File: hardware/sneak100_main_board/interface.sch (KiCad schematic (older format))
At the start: 18 parts, among them J10 Conn_01x06, SW2 SW_Push, SW3 SW_Push, SW4 SW_Push, U10 SSD1306, U11 TSOP4838

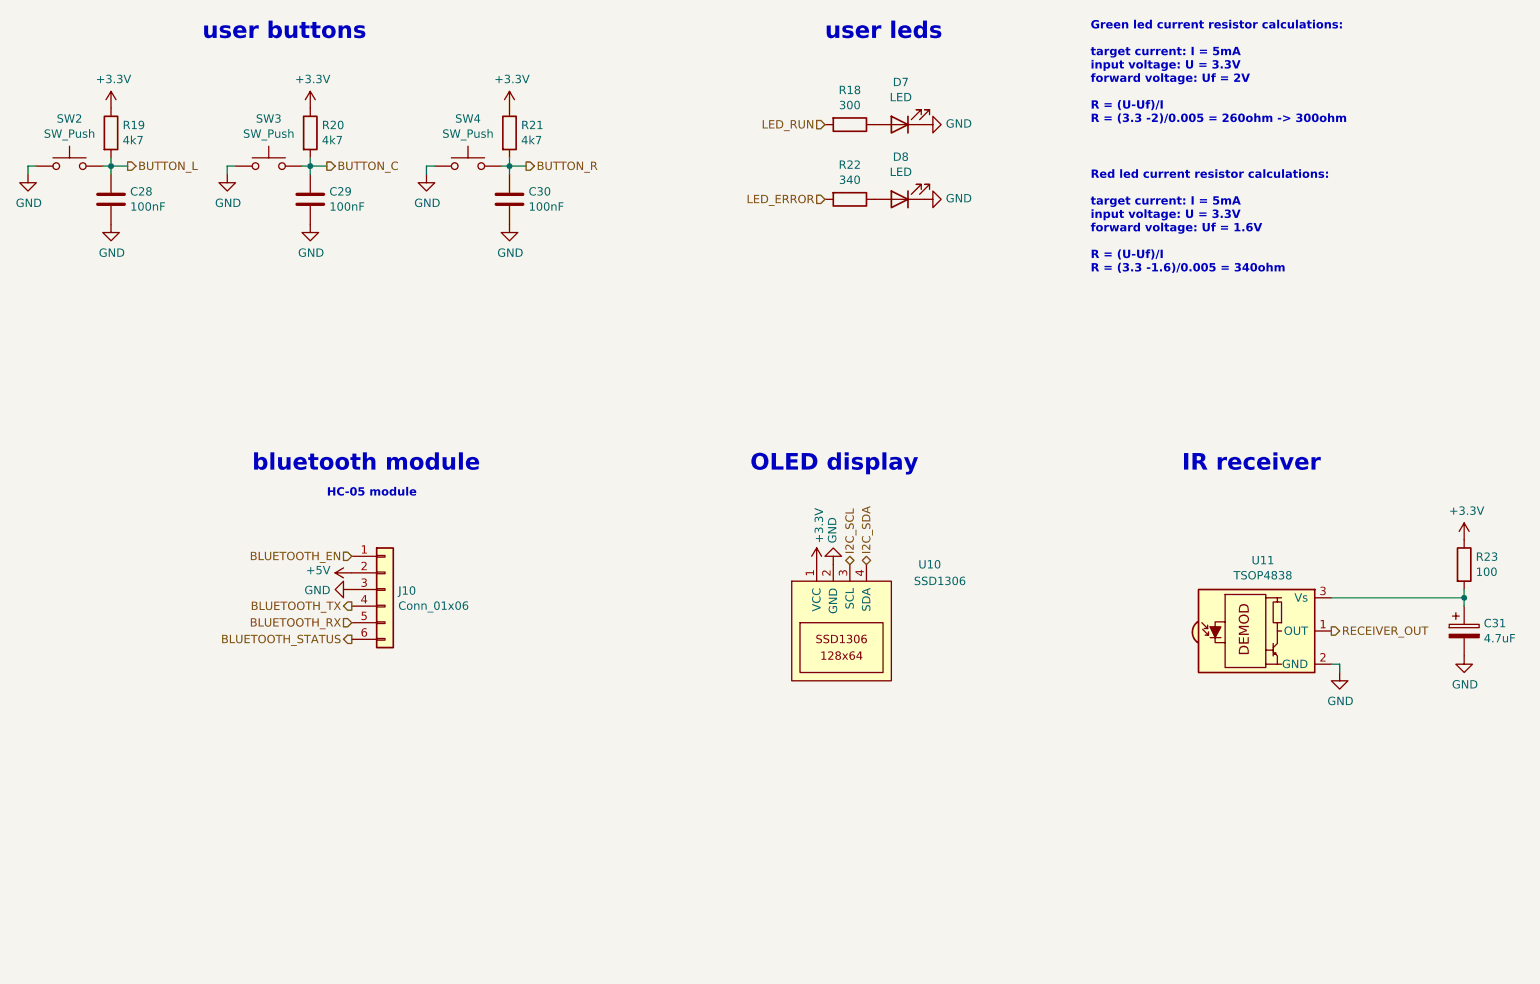
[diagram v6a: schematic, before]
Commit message: Add external proximity sensor, erase old from schematic
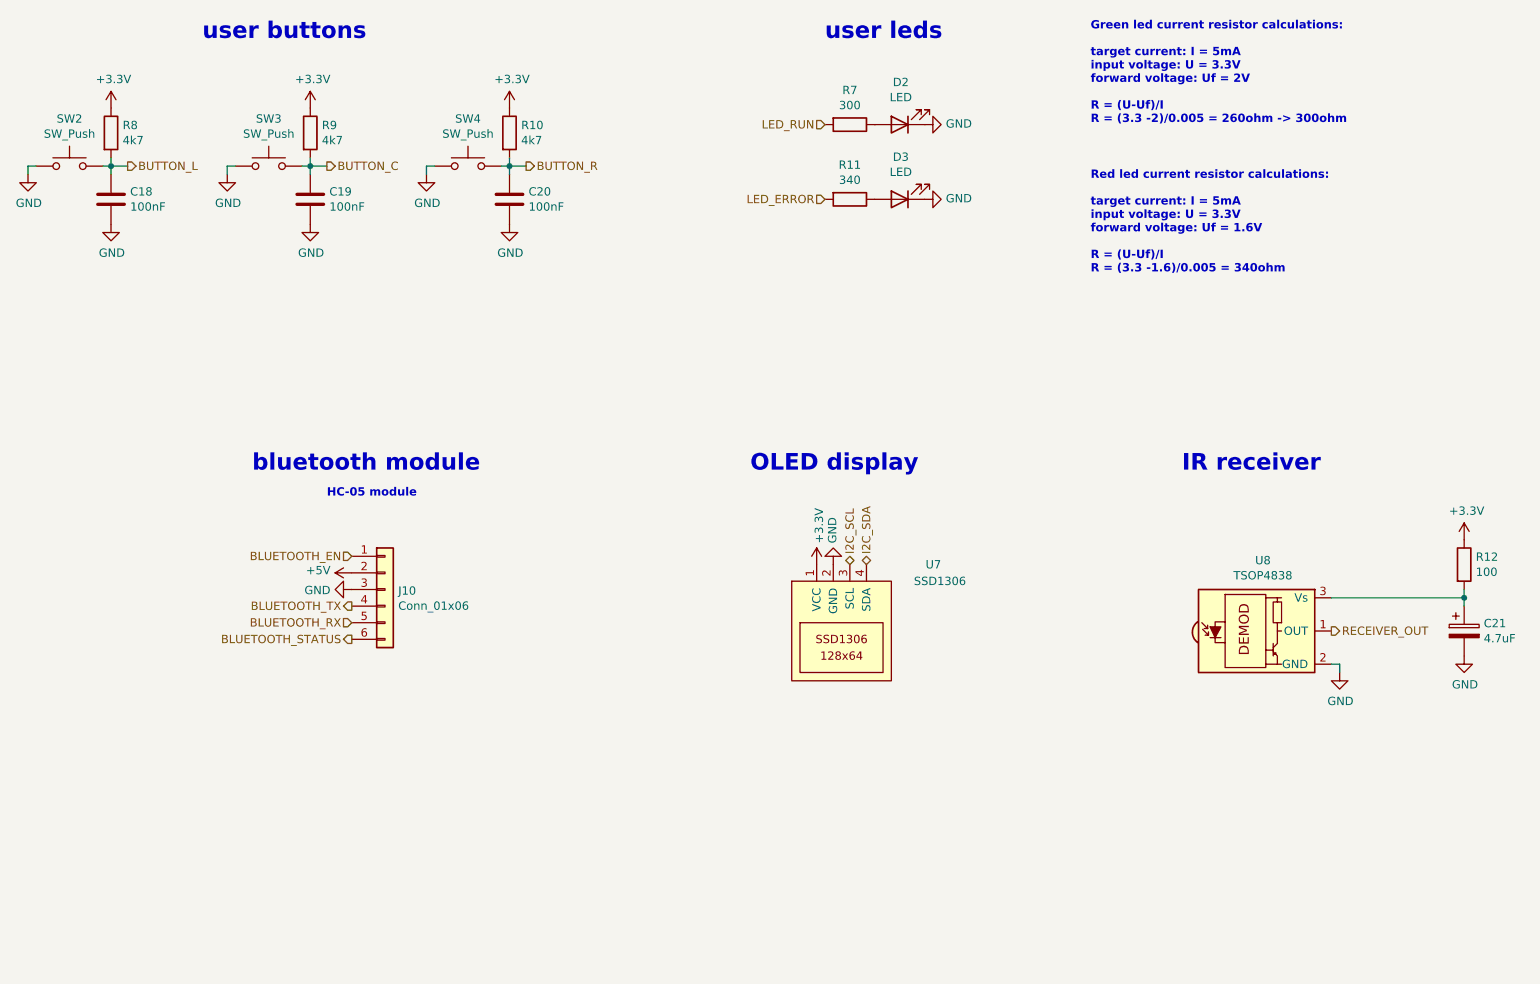
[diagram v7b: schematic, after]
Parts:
- C21: renamed from C31; footprint Capacitor_THT:CP_Radial_D5.0mm_P2.00mm -> Capacitor_Tantalum_SMD:CP_EIA-3216-18_Kemet-A
- renumbered C28 to C18, C29 to C19, C30 to C20, D7 to D2, D8 to D3, R21 to R10, R22 to R11, R23 to R12, R18 to R7, R19 to R8, R20 to R9, U10 to U7, U11 to U8
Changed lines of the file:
@@
 $Descr A4 11693 8268
 encoding utf-8
-Sheet 7 7
+Sheet 5 7
 Title ""
 Date ""
@@
 $EndComp
 $Comp
-L Device:R R19
+L Device:R R8
 U 1 1 61055001
 P 1700 1700
-F 0 "R19" H 1770 1746 50  0000 L CNN
+F 0 "R8" H 1770 1746 50  0000 L CNN
 F 1 "4k7" H 1770 1655 50  0000 L CNN
 F 2 "Resistor_SMD:R_0603_1608Metric" V 1630 1700 50  0001 C CNN
@@
 $EndComp
 $Comp
-L power:+3.3V #PWR0110
+L power:+3.3V #PWR061
 U 1 1 610558C1
 P 1700 1550
-F 0 "#PWR0110" H 1700 1400 50  0001 C CNN
+F 0 "#PWR061" H 1700 1400 50  0001 C CNN
 F 1 "+3.3V" H 1715 1723 50  0000 C CNN
 F 2 "" H 1700 1550 50  0001 C CNN
@@
 $EndComp
 $Comp
-L power:GND #PWR0114
+L power:GND #PWR065
 U 1 1 61055FD5
 P 1200 1950
-F 0 "#PWR0114" H 1200 1700 50  0001 C CNN
+F 0 "#PWR065" H 1200 1700 50  0001 C CNN
 F 1 "GND" H 1205 1777 50  0000 C CNN
 F 2 "" H 1200 1950 50  0001 C CNN
@@
 $EndComp
 $Comp
-L Device:C C28
+L Device:C C18
 U 1 1 61056486
 P 1700 2100
-F 0 "C28" H 1815 2146 50  0000 L CNN
+F 0 "C18" H 1815 2146 50  0000 L CNN
 F 1 "100nF" H 1815 2055 50  0000 L CNN
 F 2 "Capacitor_SMD:C_0603_1608Metric" H 1738 1950 50  0001 C CNN
@@
 $EndComp
 $Comp
-L power:GND #PWR0118
+L power:GND #PWR069
 U 1 1 6105698D
 P 1700 2250
-F 0 "#PWR0118" H 1700 2000 50  0001 C CNN
+F 0 "#PWR069" H 1700 2000 50  0001 C CNN
 F 1 "GND" H 1705 2077 50  0000 C CNN
 F 2 "" H 1700 2250 50  0001 C CNN
@@
 BUTTON_L
 $Comp
-L Device:LED D7
+L Device:LED D2
 U 1 1 6105F07D
 P 6450 1650
-F 0 "D7" H 6443 1395 50  0000 C CNN
+F 0 "D2" H 6443 1395 50  0000 C CNN
 F 1 "LED" H 6443 1486 50  0000 C CNN
 F 2 "LED_SMD:LED_0603_1608Metric" H 6450 1650 50  0001 C CNN
@@
 $EndComp
 $Comp
-L Device:R R18
+L Device:R R7
 U 1 1 61060DB0
 P 6150 1650
-F 0 "R18" V 5943 1650 50  0000 C CNN
+F 0 "R7" V 5943 1650 50  0000 C CNN
 F 1 "300" V 6034 1650 50  0000 C CNN
 F 2 "Resistor_SMD:R_0603_1608Metric" V 6080 1650 50  0001 C CNN
@@
 $EndComp
 $Comp
-L power:GND #PWR0113
+L power:GND #PWR064
 U 1 1 61061E6F
 P 6600 1650
-F 0 "#PWR0113" H 6600 1400 50  0001 C CNN
+F 0 "#PWR064" H 6600 1400 50  0001 C CNN
 F 1 "GND" V 6605 1522 50  0000 R CNN
 F 2 "" H 6600 1650 50  0001 C CNN
@@
 BLUETOOTH_TX
 $Comp
-L power:GND #PWR0126
+L power:GND #PWR076
 U 1 1 60F1FEEB
 P 3150 4450
-F 0 "#PWR0126" H 3150 4200 50  0001 C CNN
+F 0 "#PWR076" H 3150 4200 50  0001 C CNN
 F 1 "GND" V 3155 4322 50  0000 R CNN
 F 2 "" H 3150 4450 50  0001 C CNN
@@
 $EndComp
 $Comp
-L power:+5V #PWR0125
+L power:+5V #PWR075
 U 1 1 60F200B0
 P 3150 4350
-F 0 "#PWR0125" H 3150 4200 50  0001 C CNN
+F 0 "#PWR075" H 3150 4200 50  0001 C CNN
 F 1 "+5V" V 3165 4478 50  0000 L CNN
 F 2 "" H 3150 4350 50  0001 C CNN
@@
 IR receiver
 $Comp
-L Sneak100_kicad:TSOP4838 U11
+L Sneak100_kicad:TSOP4838 U8
 U 1 1 60F76D5D
 P 8600 4700
-F 0 "U11" H 8638 5125 50  0000 C CNN
+F 0 "U8" H 8638 5125 50  0000 C CNN
 F 1 "TSOP4838" H 8638 5034 50  0000 C CNN
 F 2 "Connector_PinHeader_2.54mm:PinHeader_1x03_P2.54mm_Vertical" H 8600 5050 50  0001 C CNN
@@
 $EndComp
 $Comp
-L power:GND #PWR0128
+L power:GND #PWR078
 U 1 1 60F7CCD5
 P 9100 4950
-F 0 "#PWR0128" H 9100 4700 50  0001 C CNN
+F 0 "#PWR078" H 9100 4700 50  0001 C CNN
 F 1 "GND" H 9105 4777 50  0000 C CNN
 F 2 "" H 9100 4950 50  0001 C CNN
@@
 $EndComp
 $Comp
-L Device:CP C31
+L Device:CP C21
 U 1 1 60F7F945
 P 9850 4700
-F 0 "C31" H 9968 4746 50  0000 L CNN
+F 0 "C21" H 9968 4746 50  0000 L CNN
 F 1 "4.7uF" H 9968 4655 50  0000 L CNN
-F 2 "Capacitor_THT:CP_Radial_D5.0mm_P2.00mm" H 9888 4550 50  0001 C CNN
+F 2 "Capacitor_Tantalum_SMD:CP_EIA-3216-18_Kemet-A" H 9888 4550 50  0001 C CNN
 F 3 "~" H 9850 4700 50  0001 C CNN
 	1    9850 4700
@@
 $EndComp
 $Comp
-L power:GND #PWR0127
+L power:GND #PWR077
 U 1 1 60F80FC7
 P 9850 4850
-F 0 "#PWR0127" H 9850 4600 50  0001 C CNN
+F 0 "#PWR077" H 9850 4600 50  0001 C CNN
 F 1 "GND" H 9855 4677 50  0000 C CNN
 F 2 "" H 9850 4850 50  0001 C CNN
@@
 $EndComp
 $Comp
-L Device:R R23
+L Device:R R12
 U 1 1 60F8B46D
 P 9850 4300
-F 0 "R23" H 9920 4346 50  0000 L CNN
+F 0 "R12" H 9920 4346 50  0000 L CNN
 F 1 "100" H 9920 4255 50  0000 L CNN
 F 2 "Resistor_SMD:R_0603_1608Metric" V 9780 4300 50  0001 C CNN
@@
 $EndComp
 $Comp
-L power:+3.3V #PWR0122
+L power:+3.3V #PWR072
 U 1 1 60F8BCE9
 P 9850 4150
-F 0 "#PWR0122" H 9850 4000 50  0001 C CNN
+F 0 "#PWR072" H 9850 4000 50  0001 C CNN
 F 1 "+3.3V" H 9865 4323 50  0000 C CNN
 F 2 "" H 9850 4150 50  0001 C CNN
@@
 $EndComp
 $Comp
-L Device:R R20
+L Device:R R9
 U 1 1 60F90EC5
 P 2900 1700
-F 0 "R20" H 2970 1746 50  0000 L CNN
+F 0 "R9" H 2970 1746 50  0000 L CNN
 F 1 "4k7" H 2970 1655 50  0000 L CNN
 F 2 "Resistor_SMD:R_0603_1608Metric" V 2830 1700 50  0001 C CNN
@@
 $EndComp
 $Comp
-L power:+3.3V #PWR0111
+L power:+3.3V #PWR062
 U 1 1 60F90ECB
 P 2900 1550
-F 0 "#PWR0111" H 2900 1400 50  0001 C CNN
+F 0 "#PWR062" H 2900 1400 50  0001 C CNN
 F 1 "+3.3V" H 2915 1723 50  0000 C CNN
 F 2 "" H 2900 1550 50  0001 C CNN
@@
 $EndComp
 $Comp
-L power:GND #PWR0115
+L power:GND #PWR066
 U 1 1 60F90ED1
 P 2400 1950
-F 0 "#PWR0115" H 2400 1700 50  0001 C CNN
+F 0 "#PWR066" H 2400 1700 50  0001 C CNN
 F 1 "GND" H 2405 1777 50  0000 C CNN
 F 2 "" H 2400 1950 50  0001 C CNN
@@
 $EndComp
 $Comp
-L Device:C C29
+L Device:C C19
 U 1 1 60F90ED7
 P 2900 2100
-F 0 "C29" H 3015 2146 50  0000 L CNN
+F 0 "C19" H 3015 2146 50  0000 L CNN
 F 1 "100nF" H 3015 2055 50  0000 L CNN
 F 2 "Capacitor_SMD:C_0603_1608Metric" H 2938 1950 50  0001 C CNN
@@
 $EndComp
 $Comp
-L power:GND #PWR0119
+L power:GND #PWR070
 U 1 1 60F90EDD
 P 2900 2250
-F 0 "#PWR0119" H 2900 2000 50  0001 C CNN
+F 0 "#PWR070" H 2900 2000 50  0001 C CNN
 F 1 "GND" H 2905 2077 50  0000 C CNN
 F 2 "" H 2900 2250 50  0001 C CNN
@@
 $EndComp
 $Comp
-L Device:R R21
+L Device:R R10
 U 1 1 60F92AB2
 P 4100 1700
-F 0 "R21" H 4170 1746 50  0000 L CNN
+F 0 "R10" H 4170 1746 50  0000 L CNN
 F 1 "4k7" H 4170 1655 50  0000 L CNN
 F 2 "Resistor_SMD:R_0603_1608Metric" V 4030 1700 50  0001 C CNN
@@
 $EndComp
 $Comp
-L power:+3.3V #PWR0112
+L power:+3.3V #PWR063
 U 1 1 60F92AB8
 P 4100 1550
-F 0 "#PWR0112" H 4100 1400 50  0001 C CNN
+F 0 "#PWR063" H 4100 1400 50  0001 C CNN
 F 1 "+3.3V" H 4115 1723 50  0000 C CNN
 F 2 "" H 4100 1550 50  0001 C CNN
@@
 $EndComp
 $Comp
-L power:GND #PWR0116
+L power:GND #PWR067
 U 1 1 60F92ABE
 P 3600 1950
-F 0 "#PWR0116" H 3600 1700 50  0001 C CNN
+F 0 "#PWR067" H 3600 1700 50  0001 C CNN
 F 1 "GND" H 3605 1777 50  0000 C CNN
 F 2 "" H 3600 1950 50  0001 C CNN
@@
 $EndComp
 $Comp
-L Device:C C30
+L Device:C C20
 U 1 1 60F92AC4
 P 4100 2100
-F 0 "C30" H 4215 2146 50  0000 L CNN
+F 0 "C20" H 4215 2146 50  0000 L CNN
 F 1 "100nF" H 4215 2055 50  0000 L CNN
 F 2 "Capacitor_SMD:C_0603_1608Metric" H 4138 1950 50  0001 C CNN
@@
 $EndComp
 $Comp
-L power:GND #PWR0120
+L power:GND #PWR071
 U 1 1 60F92ACA
 P 4100 2250
-F 0 "#PWR0120" H 4100 2000 50  0001 C CNN
+F 0 "#PWR071" H 4100 2000 50  0001 C CNN
 F 1 "GND" H 4105 2077 50  0000 C CNN
 F 2 "" H 4100 2250 50  0001 C CNN
@@
 BUTTON_R
 $Comp
-L power:+3.3V #PWR0123
+L power:+3.3V #PWR073
 U 1 1 60FBF32E
 P 5950 4300
-F 0 "#PWR0123" H 5950 4150 50  0001 C CNN
+F 0 "#PWR073" H 5950 4150 50  0001 C CNN
 F 1 "+3.3V" V 5965 4428 50  0000 L CNN
 F 2 "" H 5950 4300 50  0001 C CNN
@@
 $EndComp
 $Comp
-L power:GND #PWR0124
+L power:GND #PWR074
 U 1 1 60FBFC20
 P 6050 4300
-F 0 "#PWR0124" H 6050 4050 50  0001 C CNN
+F 0 "#PWR074" H 6050 4050 50  0001 C CNN
 F 1 "GND" V 6055 4172 50  0000 R CNN
 F 2 "" H 6050 4300 50  0001 C CNN
@@
 $EndComp
 $Comp
-L Device:LED D8
+L Device:LED D3
 U 1 1 60FD241C
 P 6450 2100
-F 0 "D8" H 6443 1845 50  0000 C CNN
+F 0 "D3" H 6443 1845 50  0000 C CNN
 F 1 "LED" H 6443 1936 50  0000 C CNN
 F 2 "LED_SMD:LED_0603_1608Metric" H 6450 2100 50  0001 C CNN
@@
 $EndComp
 $Comp
-L Device:R R22
+L Device:R R11
 U 1 1 60FD2422
 P 6150 2100
-F 0 "R22" V 5943 2100 50  0000 C CNN
+F 0 "R11" V 5943 2100 50  0000 C CNN
 F 1 "340" V 6034 2100 50  0000 C CNN
 F 2 "Resistor_SMD:R_0603_1608Metric" V 6080 2100 50  0001 C CNN
@@
 $EndComp
 $Comp
-L power:GND #PWR0117
+L power:GND #PWR068
 U 1 1 60FD2428
 P 6600 2100
-F 0 "#PWR0117" H 6600 1850 50  0001 C CNN
+F 0 "#PWR068" H 6600 1850 50  0001 C CNN
 F 1 "GND" V 6605 1972 50  0000 R CNN
 F 2 "" H 6600 2100 50  0001 C CNN
@@
 HC-05 module
 $Comp
-L Sneak100_kicad:SSD1306 U10
+L Sneak100_kicad:SSD1306 U7
 U 1 1 6101ACF5
 P 6100 4650
-F 0 "U10" H 6700 5000 50  0000 R CNN
+F 0 "U7" H 6700 5000 50  0000 R CNN
 F 1 "SSD1306" H 6850 4900 50  0000 R CNN
 F 2 "sneak100_lib:SSD1306_module" H 5950 4600 50  0001 C CNN

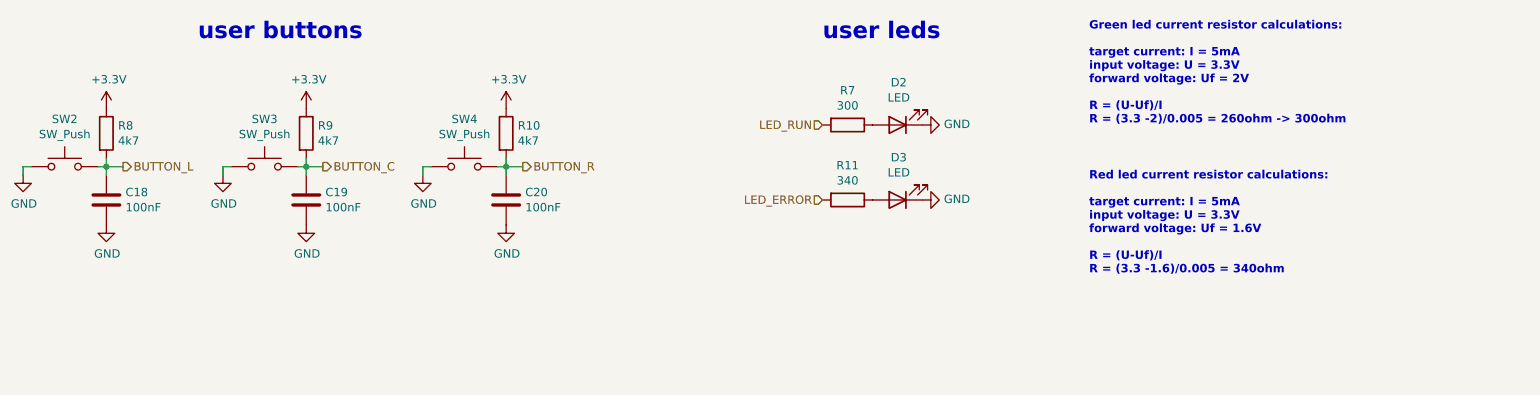
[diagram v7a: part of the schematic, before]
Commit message: component list and values fix
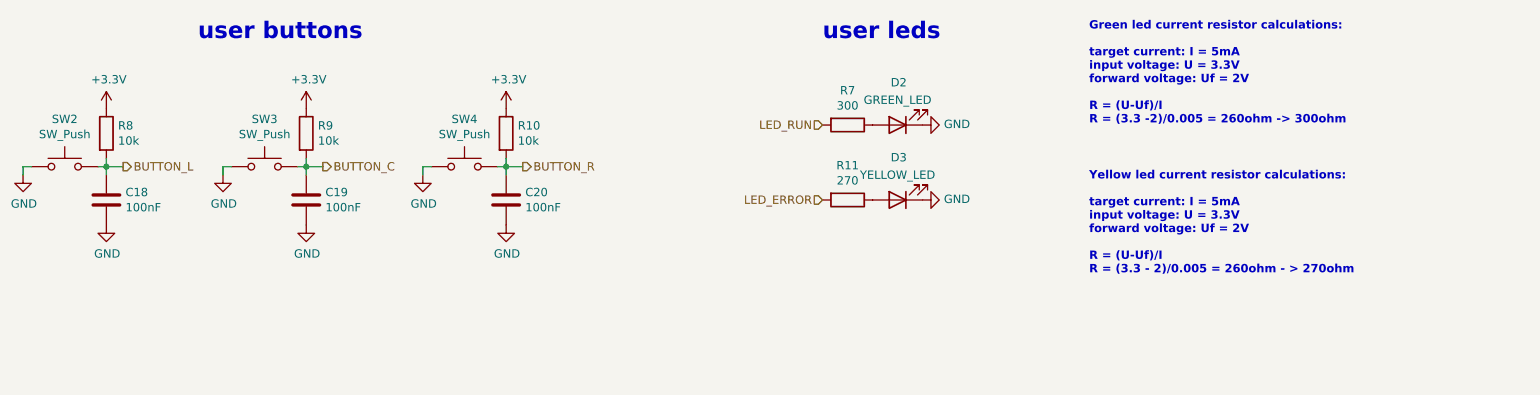
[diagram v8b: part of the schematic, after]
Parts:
- D2: value LED -> GREEN_LED
- D3: value LED -> YELLOW_LED
- R10, R8, R9: value 4k7 -> 10k
- R11: value 340 -> 270
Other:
- note added: "Yellow led current resistor calculations:\n\ntarget current: I = 5mA\ninput voltage: U = 3.3V\nforward voltage: Uf = 2V\n\nR = (U-Uf)/I\nR = (3.3 - 2)/0.005 = 260ohm - > 270ohm"
- note removed: "Red led current resistor calculations:\n\ntarget current: I = 5mA\ninput voltage: U = 3.3V\nforward voltage: Uf = 1.6V\n\nR = (U-Uf)/I\nR = (3.3 -1.6)/0.005 = 340ohm"
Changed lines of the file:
@@
 P 1700 1700
 F 0 "R8" H 1770 1746 50  0000 L CNN
-F 1 "4k7" H 1770 1655 50  0000 L CNN
+F 1 "10k" H 1770 1655 50  0000 L CNN
 F 2 "Resistor_SMD:R_0603_1608Metric" V 1630 1700 50  0001 C CNN
 F 3 "~" H 1700 1700 50  0001 C CNN
@@
 P 6450 1650
 F 0 "D2" H 6443 1395 50  0000 C CNN
-F 1 "LED" H 6443 1486 50  0000 C CNN
+F 1 "GREEN_LED" H 6450 1500 50  0000 C CNN
 F 2 "LED_SMD:LED_0603_1608Metric" H 6450 1650 50  0001 C CNN
 F 3 "~" H 6450 1650 50  0001 C CNN
@@
 P 2900 1700
 F 0 "R9" H 2970 1746 50  0000 L CNN
-F 1 "4k7" H 2970 1655 50  0000 L CNN
+F 1 "10k" H 2970 1655 50  0000 L CNN
 F 2 "Resistor_SMD:R_0603_1608Metric" V 2830 1700 50  0001 C CNN
 F 3 "~" H 2900 1700 50  0001 C CNN
@@
 P 4100 1700
 F 0 "R10" H 4170 1746 50  0000 L CNN
-F 1 "4k7" H 4170 1655 50  0000 L CNN
+F 1 "10k" H 4170 1655 50  0000 L CNN
 F 2 "Resistor_SMD:R_0603_1608Metric" V 4030 1700 50  0001 C CNN
 F 3 "~" H 4100 1700 50  0001 C CNN
@@
 P 6450 2100
 F 0 "D3" H 6443 1845 50  0000 C CNN
-F 1 "LED" H 6443 1936 50  0000 C CNN
+F 1 "YELLOW_LED" H 6450 1950 50  0000 C CNN
 F 2 "LED_SMD:LED_0603_1608Metric" H 6450 2100 50  0001 C CNN
 F 3 "~" H 6450 2100 50  0001 C CNN
@@
 P 6150 2100
 F 0 "R11" V 5943 2100 50  0000 C CNN
-F 1 "340" V 6034 2100 50  0000 C CNN
+F 1 "270" V 6034 2100 50  0000 C CNN
 F 2 "Resistor_SMD:R_0603_1608Metric" V 6080 2100 50  0001 C CNN
 F 3 "~" H 6150 2100 50  0001 C CNN
@@
 LED_ERROR
 Text Notes 7600 2550 0    50   ~ 10
-Red led current resistor calculations:\n\ntarget current: I = 5mA\ninput voltage: U = 3.3V\nforward voltage: Uf = 1.6V\n\nR = (U-Uf)/I\nR = (3.3 -1.6)/0.005 = 340ohm
+Yellow led current resistor calculations:\n\ntarget current: I = 5mA\ninput voltage: U = 3.3V\nforward voltage: Uf = 2V\n\nR = (U-Uf)/I\nR = (3.3 - 2)/0.005 = 260ohm - > 270ohm
 Text Notes 3000 3900 0    50   ~ 10
 HC-05 module
